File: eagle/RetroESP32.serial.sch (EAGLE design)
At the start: 68 parts, among them J1 AUDIO_JACK_3.5MM_KIT, J2 SPKR, J3 Batt Conn, J5 503182-1852_503182-1852, J6 USB4110-GF-A, Q3 DMG3415U-7, Q4 mmbt2222, Q5 mmbt2222, U1 ESP32-WROVER_ESP32-WROVER, U3 AP2112-3.3, U4 MCP73831T-2ACI/OT, U6 LM4875

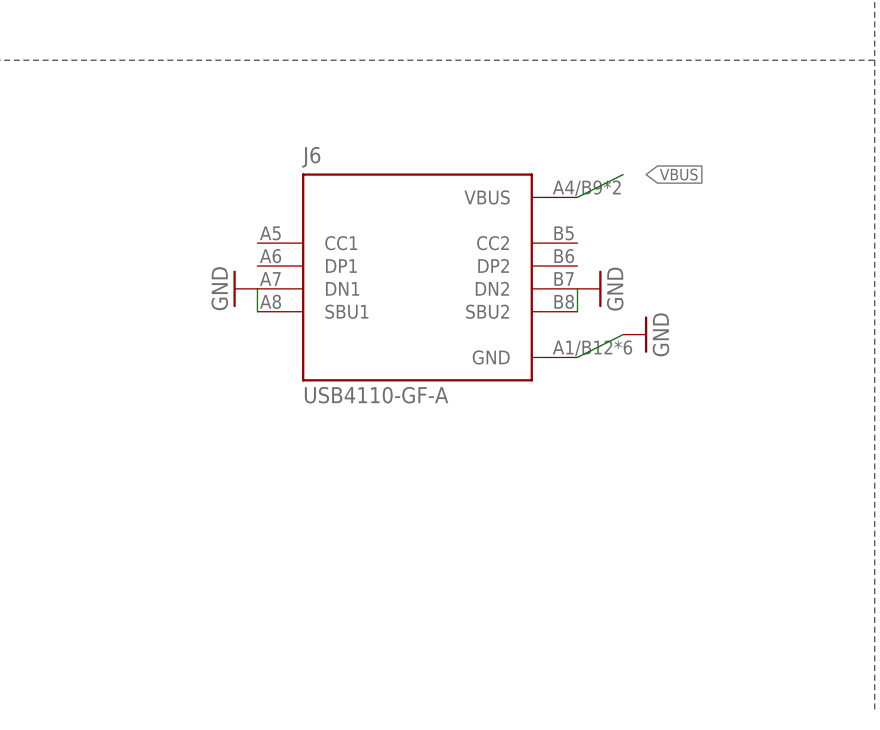
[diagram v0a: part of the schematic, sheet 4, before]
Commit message: updated CC1/2 pins
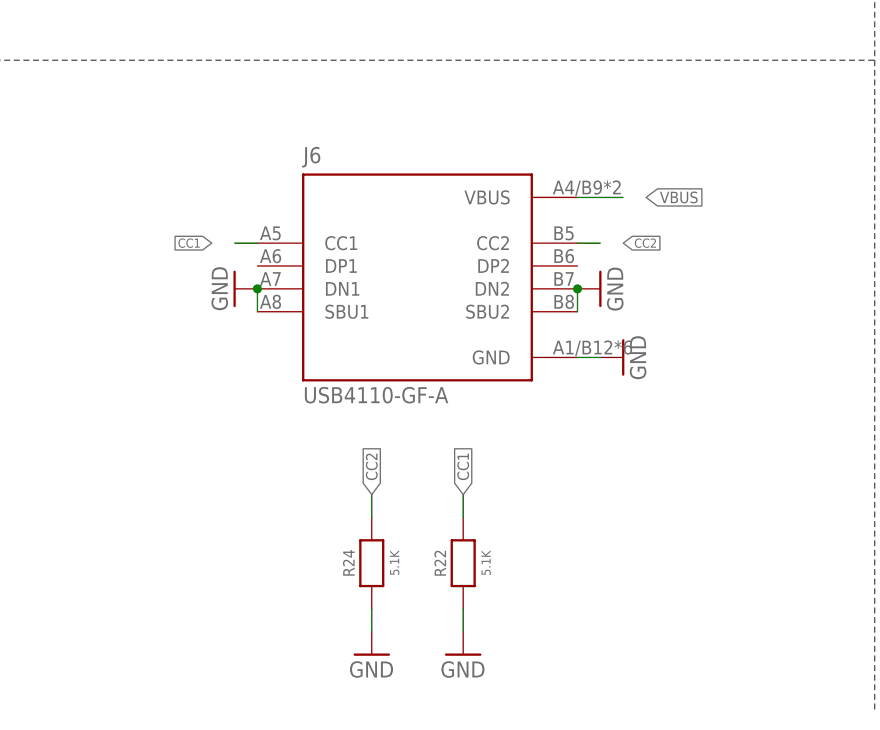
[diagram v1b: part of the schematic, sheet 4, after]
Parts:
- added R22, R24: 5.1K, RetroESP32:RESISTOR0603MINI
- R1: value 4.7K -> 1.5K; MPN ERJ-PA3J472V -> ERJ-PA3J152V
- U3: value AP2112-3.3 -> XC6210B332MR-G; MPN AP2112K-3.3TRG1 -> XC6210B332MR-G
- U4: value MCP73831T-2ACI/OT -> MCP73832T-2ACI/OT; MPN MCP73831T-2ACI/OT -> MCP73832T-2ACI/OT
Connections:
- new net CC1: J6.CC1, R22.2
- new net CC2: J6.CC2, R24.2
- net GND: now also J6.DN1, J6.DN2, R22.1, R24.1

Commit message: Added new DXF and BOM
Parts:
- U$11: MPN FH34SRJ-45S-0.5SH(50) -> 0541324562
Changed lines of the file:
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@@
 <part name="U$17" library="RetroESP32" library_urn="urn:adsk.eagle:library:12566846" deviceset="MGB-001" device="MGB-001-ESP32-LITE" package3d_urn="urn:adsk.eagle:package:25781132/2" value="MGB-001MGB-001-ESP32-LITE"/>
 <part name="U$11" library="RetroESP32" library_urn="urn:adsk.eagle:library:12566846" deviceset="KD026LQTMA008" device="" package3d_urn="urn:adsk.eagle:package:21234581/3">
-<attribute name="MPN" value="FH34SRJ-45S-0.5SH(50)"/>
+<attribute name="MPN" value="0541324562"/>
 </part>
 <part name="GND10" library="RetroESP32" library_urn="urn:adsk.eagle:library:12566846" deviceset="GND" device=""/>
